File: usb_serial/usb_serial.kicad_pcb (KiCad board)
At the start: 2 copper layers, 17 parts, among them P1 USB_OTG, P2 CONN_01X04, P3 CONN_01X04, Q1 S8050, Q2 S8050, U1 CH340G, X1 CRYSTAL_SMD

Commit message: Unsaved changes
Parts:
- C2: value C -> 100nF
- D1: value D_Schottky -> D_Schottky_x2_ACom_AKK; footprint Diodes_SMD:DO-214AB_Handsoldering -> TO_SOT_Packages_SMD:SOT-23
- moved P2 37.1 mm to (147.2, 78.5)
- moved P3 32.0 mm to (167.6, 78.5)
- moved D1 1.84 mm to (190.6, 121.7)
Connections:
- D1 pad 1: +5V -> +5P
- D1 pad 2: +5P -> Net-(D1-Pad2)
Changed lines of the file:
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@@
     (zones 0)
     (modules 17)
-    (nets 25)
+    (nets 26)
   )
   (page A4)
@@
   (net 23 "Net-(U1-Pad10)")
   (net 24 "Net-(U1-Pad9)")
+  (net 25 "Net-(D1-Pad2)")
   (net_class Default "This is the default net class."
     (clearance 0.2)
@@
     (add_net "Net-(C2-Pad1)")
     (add_net "Net-(C3-Pad1)")
+    (add_net "Net-(D1-Pad2)")
     (add_net "Net-(P1-Pad4)")
     (add_net "Net-(Q1-Pad2)")
@@
       (effects (font (size 1 1) (thickness 0.15)))
     )
-    (fp_text value C (at 0 1.7) (layer F.Fab)
+    (fp_text value 100nF (at 0 1.7) (layer F.Fab)
       (effects (font (size 1 1) (thickness 0.15)))
     )
@@
       (at (xyz 0 0 0))
       (scale (xyz 1 1 1))
-      (rotate (xyz 0 0 180))
-    )
-  )
-  (module Diodes_SMD:DO-214AB_Handsoldering (layer F.Cu)
-    (at 191.387001 120.079)
-    (descr "Jedec DO-214AB diode package. Designed according to Fairchild SS32 datasheet.")
-    (tags "DO-214AB diode Handsoldering")
-    (attr smd)
-    (fp_text reference D1 (at 0 -4.2) (layer F.SilkS)
-      (effects (font (size 1 1) (thickness 0.15)))
-    )
-    (fp_text value D_Schottky (at 0 4.6) (layer F.Fab)
-      (effects (font (size 1 1) (thickness 0.15)))
-    )
-    (fp_line (start -6.15 -3.45) (end 6.15 -3.45) (layer F.CrtYd) (width 0.05))
-    (fp_line (start 6.15 -3.45) (end 6.15 3.45) (layer F.CrtYd) (width 0.05))
-    (fp_line (start 6.15 3.45) (end -6.15 3.45) (layer F.CrtYd) (width 0.05))
-    (fp_line (start -6.15 3.45) (end -6.15 -3.45) (layer F.CrtYd) (width 0.05))
-    (fp_line (start 3.5 3.2) (end -5.8 3.2) (layer F.SilkS) (width 0.15))
-    (fp_line (start -5.8 -3.2) (end 3.5 -3.2) (layer F.SilkS) (width 0.15))
-    (pad 2 smd rect (at 4.1 0) (size 3.6 3.2) (layers F.Cu F.Paste F.Mask)
-      (net 6 +5P))
-    (pad 1 smd rect (at -4.1 0) (size 3.6 3.2) (layers F.Cu F.Paste F.Mask)
-      (net 5 +5V))
-    (model Diodes_SMD.3dshapes/DO-214AB_Handsoldering.wrl
-      (at (xyz 0 0 0))
-      (scale (xyz 0.39 0.39 0.39))
       (rotate (xyz 0 0 180))
     )
@@
   )
   (module Pin_Headers:Pin_Header_Straight_1x04 (layer F.Cu)
-    (at 169.700333 108.079)
+    (at 147.25 78.5)
     (descr "Through hole pin header")
     (tags "pin header")
@@
   )
   (module Pin_Headers:Pin_Header_Straight_1x04 (layer F.Cu)
-    (at 179.910333 108.079)
+    (at 167.57 78.5)
     (descr "Through hole pin header")
     (tags "pin header")
@@
       (at (xyz 0 0 0))
       (scale (xyz 1 1 1))
+      (rotate (xyz 0 0 0))
+    )
+  )
+  (module TO_SOT_Packages_SMD:SOT-23 (layer F.Cu)
+    (at 190.58 121.73)
+    (descr "SOT-23, Standard")
+    (tags SOT-23)
+    (attr smd)
+    (fp_text reference D1 (at 0 -2.25) (layer F.SilkS)
+      (effects (font (size 1 1) (thickness 0.15)))
+    )
+    (fp_text value D_Schottky_x2_ACom_AKK (at 0 2.3) (layer F.Fab)
+      (effects (font (size 1 1) (thickness 0.15)))
+    )
+    (fp_line (start -1.65 -1.6) (end 1.65 -1.6) (layer F.CrtYd) (width 0.05))
+    (fp_line (start 1.65 -1.6) (end 1.65 1.6) (layer F.CrtYd) (width 0.05))
+    (fp_line (start 1.65 1.6) (end -1.65 1.6) (layer F.CrtYd) (width 0.05))
+    (fp_line (start -1.65 1.6) (end -1.65 -1.6) (layer F.CrtYd) (width 0.05))
+    (fp_line (start 1.29916 -0.65024) (end 1.2509 -0.65024) (layer F.SilkS) (width 0.15))
+    (fp_line (start -1.49982 0.0508) (end -1.49982 -0.65024) (layer F.SilkS) (width 0.15))
+    (fp_line (start -1.49982 -0.65024) (end -1.2509 -0.65024) (layer F.SilkS) (width 0.15))
+    (fp_line (start 1.29916 -0.65024) (end 1.49982 -0.65024) (layer F.SilkS) (width 0.15))
+    (fp_line (start 1.49982 -0.65024) (end 1.49982 0.0508) (layer F.SilkS) (width 0.15))
+    (pad 1 smd rect (at -0.95 1.00076) (size 0.8001 0.8001) (layers F.Cu F.Paste F.Mask)
+      (net 6 +5P))
+    (pad 2 smd rect (at 0.95 1.00076) (size 0.8001 0.8001) (layers F.Cu F.Paste F.Mask)
+      (net 25 "Net-(D1-Pad2)"))
+    (pad 3 smd rect (at 0 -0.99822) (size 0.8001 0.8001) (layers F.Cu F.Paste F.Mask)
+      (net 5 +5V))
+    (model TO_SOT_Packages_SMD.3dshapes/SOT-23.wrl
+      (at (xyz 0 0 0))
+      (scale (xyz 1 1 1))

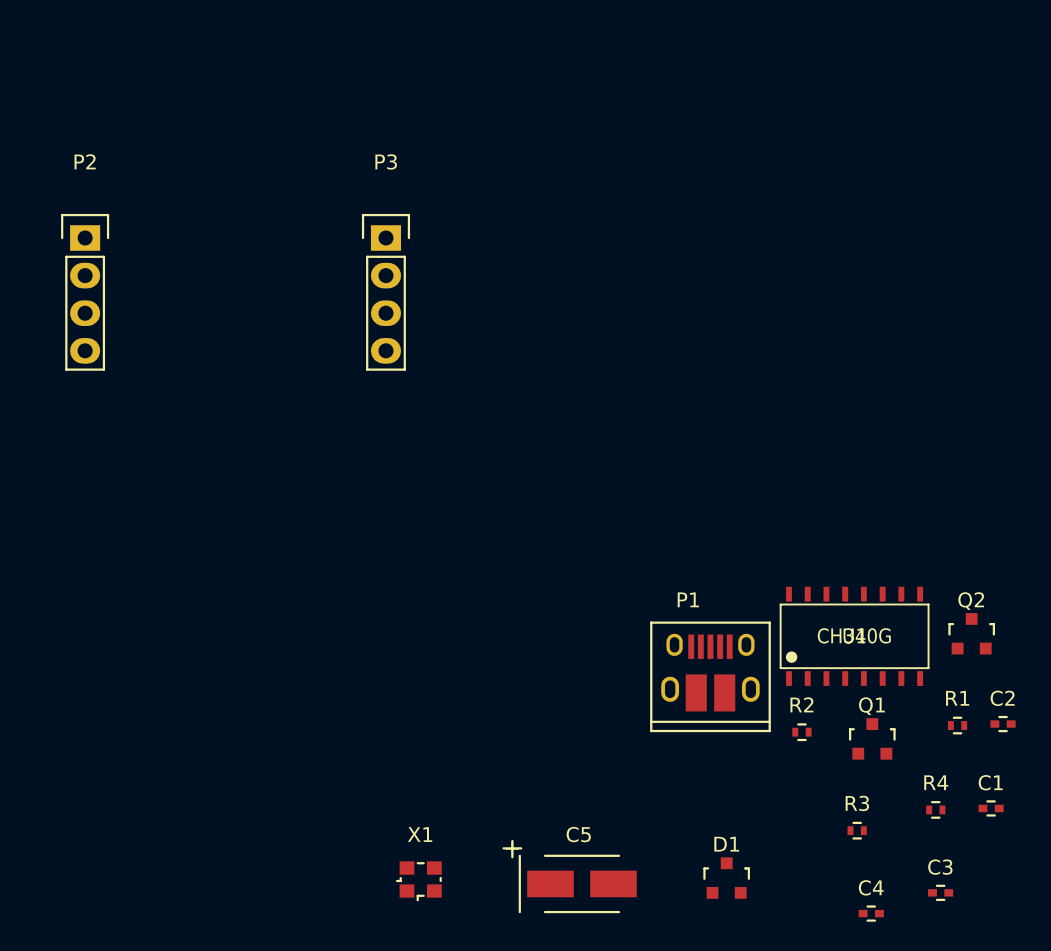
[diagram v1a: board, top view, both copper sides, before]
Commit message: Fixed S8050 footprints. USB PCB v0. Pending GND filled zone.
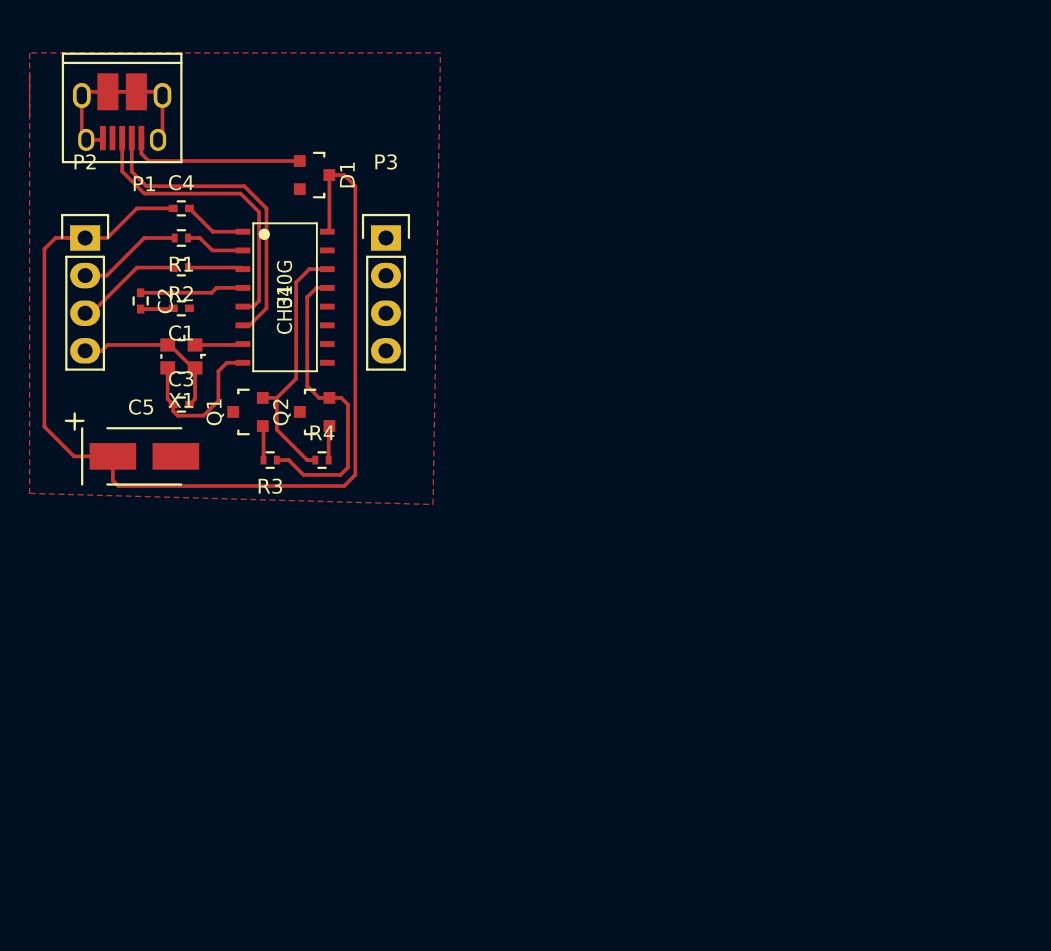
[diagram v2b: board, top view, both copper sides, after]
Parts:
- Q1, Q2: footprint TO_SOT_Packages_SMD:SOT-23 -> SOT-23_S8050:SOT-23_S8050
- moved C4 66.6 mm to (153.8, 76.5)
- moved C2 64.9 mm to (151.0, 82.8), turned to 270 degrees
- moved C1 64.3 mm to (153.8, 83.2), turned to 180 degrees
- moved R1 61.9 mm to (153.8, 78.5), turned to 180 degrees
- moved C3 61.0 mm to (153.8, 89.8)
- moved D1 55.0 mm to (162.8, 74.2), turned to 270 degrees
- moved P1 54.5 mm to (149.8, 70.2), turned to 180 degrees
- moved R2 52.4 mm to (153.8, 80.5), turned to 180 degrees
- moved R4 47.7 mm to (163.2, 93.5)
- moved Q1 47.6 mm to (158.2, 90.2), turned to 90 degrees
- moved R3 46.9 mm to (159.8, 93.5), turned to 180 degrees
- moved Q2 46.8 mm to (162.8, 90.2), turned to 90 degrees
- moved U1 44.8 mm to (160.8, 82.5), turned to 270 degrees
- moved C5 41.3 mm to (151.2, 93.2)
- moved X1 38.9 mm to (153.8, 86.5), turned to 180 degrees
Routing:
- net +5V: track 0.00 -> 71.2 mm
- net Earth: track 0.00 -> 30.8 mm
- net D_NEG: track 0.00 -> 21.2 mm
- net DTR: track 0.00 -> 20.6 mm
- net D_POS: track 0.00 -> 19.9 mm
- net RTS: track 0.00 -> 17.4 mm
- net +5P: track 0.00 -> 12.0 mm
- net Net-(C3-Pad1): track 0.00 -> 10.6 mm
- net RX: track 0.00 -> 7.33 mm
- net TX: track 0.00 -> 7.10 mm
- net Net-(C2-Pad1): track 0.00 -> 7.04 mm
- net Net-(R1-Pad1): track 0.00 -> 4.05 mm
- net Net-(R2-Pad1): track 0.00 -> 3.75 mm
- net Net-(C1-Pad1): track 0.00 -> 3.25 mm
- net Net-(Q2-Pad2): track 0.00 -> 2.39 mm
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- added copper zone on F.Cu, net Earth

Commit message: Breakout USB v0 done.
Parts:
- moved C4 0.50 mm to (153.8, 77.0)
- moved R1 0.50 mm to (153.8, 79.0)
- moved R2 0.50 mm to (153.8, 81.0)
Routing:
- net Earth: track 30.8 -> 41.3 mm
- net +5V: track 71.2 -> 69.7 mm
- net D_NEG: track 21.2 -> 20.7 mm
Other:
- board outline added: 25.2 x 30.5 mm

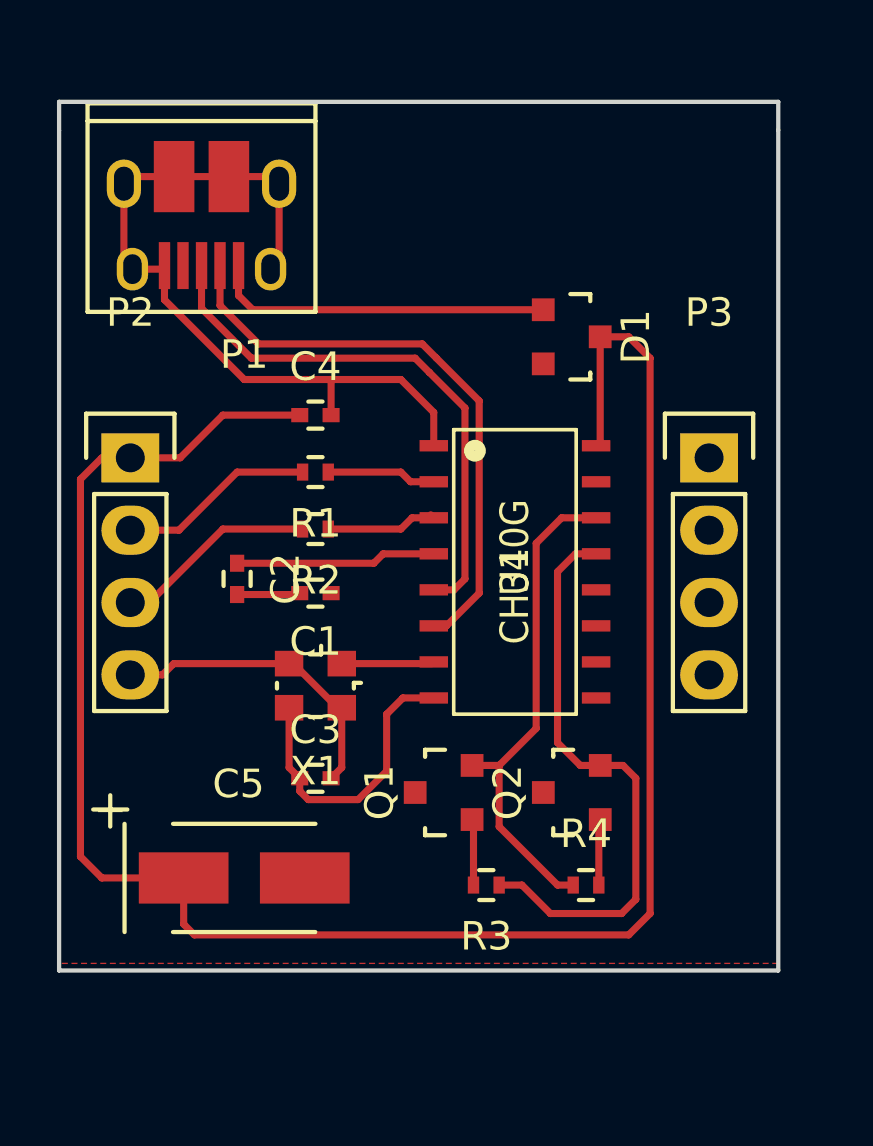
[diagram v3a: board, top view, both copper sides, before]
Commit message: Mounting holes & silkscreen with labels
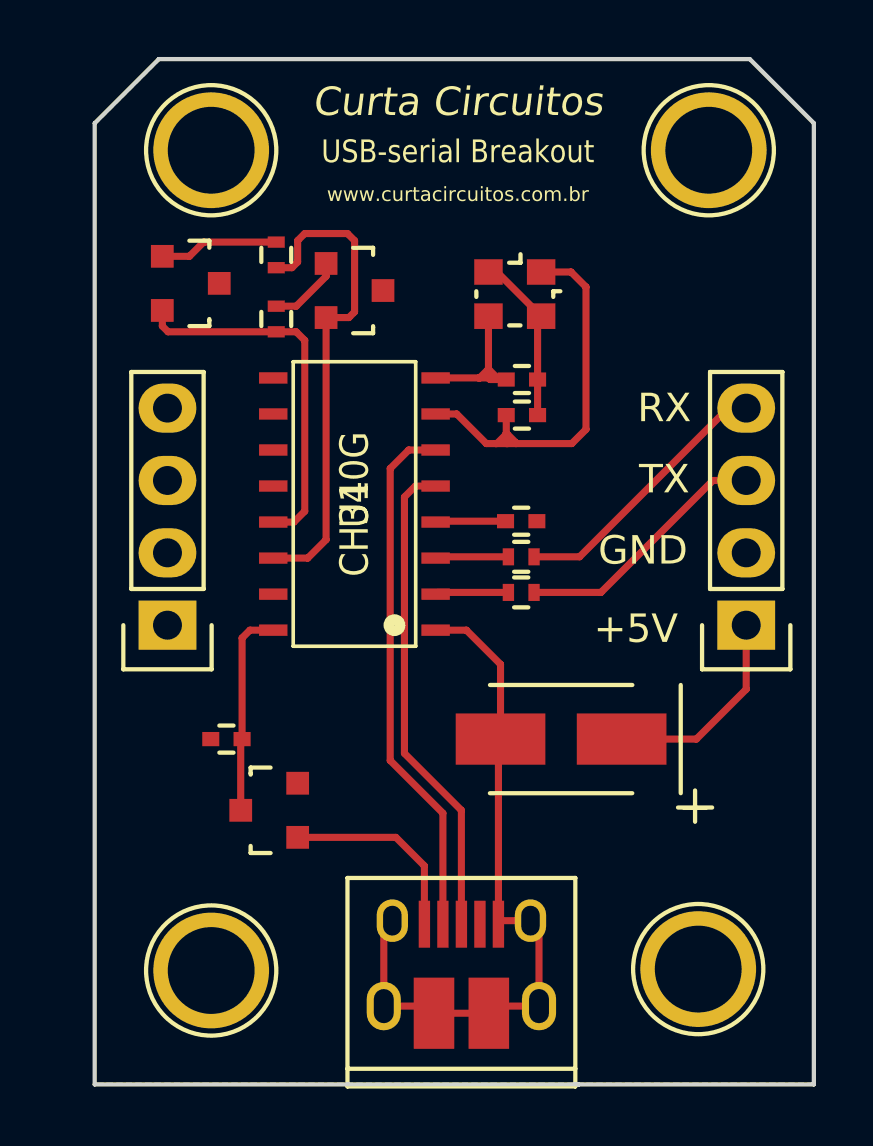
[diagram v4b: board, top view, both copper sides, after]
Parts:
- added REF**: 1pin, Connect:1pin, F.Cu at (150.1, 67.7)
- added REF**: 1pin, Connect:1pin, F.Cu at (167.6, 67.7)
- added REF**: 1pin, Connect:1pin, F.Cu at (167.2, 96.5)
- added REF**: 1pin, Connect:1pin, F.Cu at (150.1, 96.5)
- moved P1 27.7 mm to (158.9, 96.4), turned to 0 degrees
- moved R4 24.7 mm to (152.4, 71.4), turned to 90 degrees
- moved P2 22.4 mm to (168.9, 84.4), turned to 180 degrees
- moved Q2 22.3 mm to (149.4, 72.4), turned to 270 degrees
- moved R3 21.2 mm to (152.4, 73.6), turned to 90 degrees
- moved P3 19.9 mm to (148.6, 84.4), turned to 180 degrees
- moved D1 19.7 mm to (152.1, 90.9), turned to 90 degrees
- moved Q1 17.9 mm to (155.1, 72.6), turned to 270 degrees
- moved C3 15.8 mm to (161.0, 75.8)
- moved X1 15.4 mm to (160.8, 72.8)
- moved C5 12.1 mm to (162.4, 88.4), turned to 180 degrees
- moved C4 11.8 mm to (150.6, 88.4), turned to 180 degrees
- moved C2 10.2 mm to (161.0, 80.7), turned to 0 degrees
- moved C1 9.57 mm to (161.0, 77.0), turned to 0 degrees
- moved R1 8.37 mm to (161.0, 83.2), turned to 0 degrees
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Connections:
- P2 pad 2: TX -> Earth
- P2 pad 3: RX -> TX
- P2 pad 4: Earth -> RX
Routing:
- net +5V: track 69.7 -> 14.6 mm
- net Net-(C1-Pad1): track 3.25 -> 14.8 mm
- net Earth: track 41.3 -> 31.1 mm
- net DTR: track 20.6 -> 13.0 mm
- net +5P: track 12.0 -> 6.91 mm
- net Net-(C2-Pad1): track 7.04 -> 2.47 mm
- net Net-(C3-Pad1): track 10.6 -> 6.29 mm
- net D_POS: track 19.5 -> 17.1 mm
- net TX: track 6.89 -> 9.08 mm
- net D_NEG: track 20.7 -> 18.6 mm
- net RX: track 7.54 -> 9.61 mm
- net Net-(Q2-Pad2): track 2.39 -> 4.21 mm
- net Net-(R2-Pad1): track 4.02 -> 2.57 mm
- net Net-(R1-Pad1): track 3.85 -> 2.58 mm
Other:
- board size 25.2 x 30.5 mm -> 25.2 x 36 mm
- board text added: "+5V"
- board text added: "Curta Circuitos"
- board text added: "GND"
- board text added: "RX"
- board text added: "TX"
- board text added: "USB-serial Breakout"
- board text added: "www.curtacircuitos.com.br"

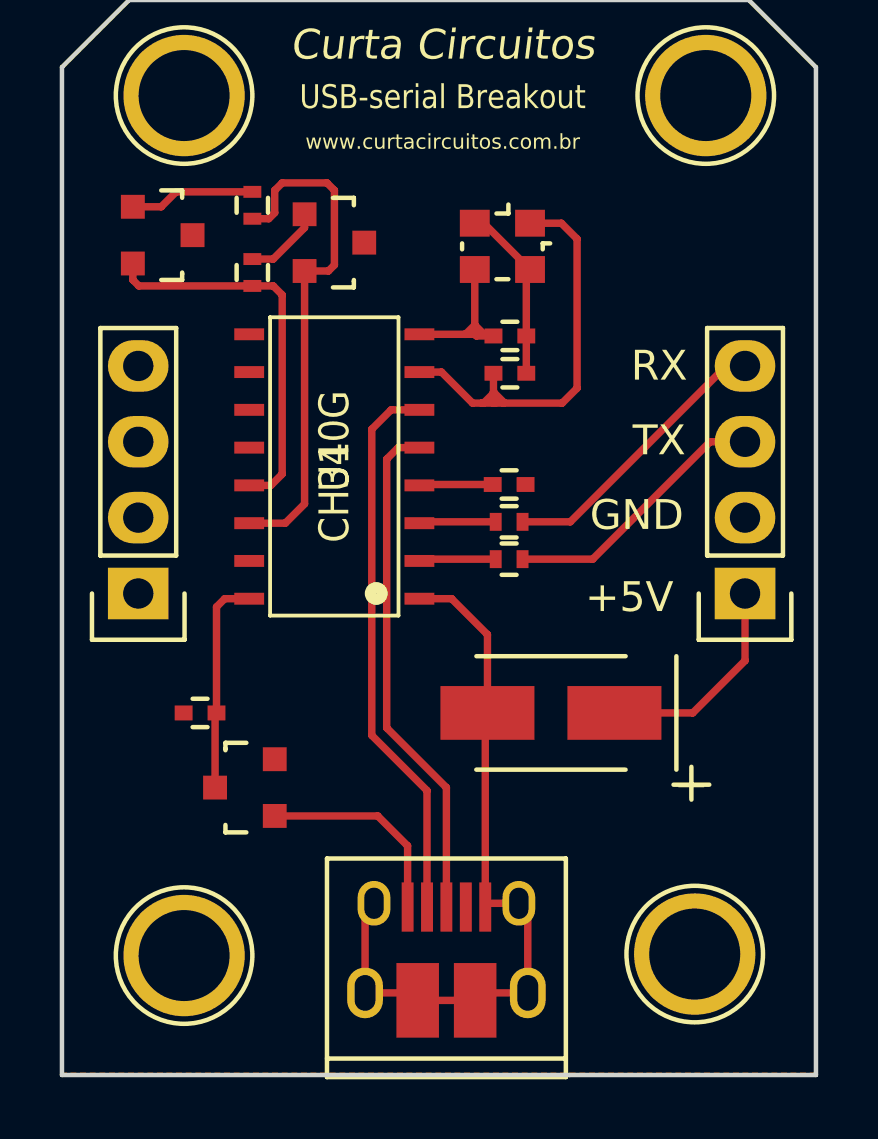
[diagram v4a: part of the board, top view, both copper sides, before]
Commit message: Expanded pin headers and minor fixes. Pics updated.
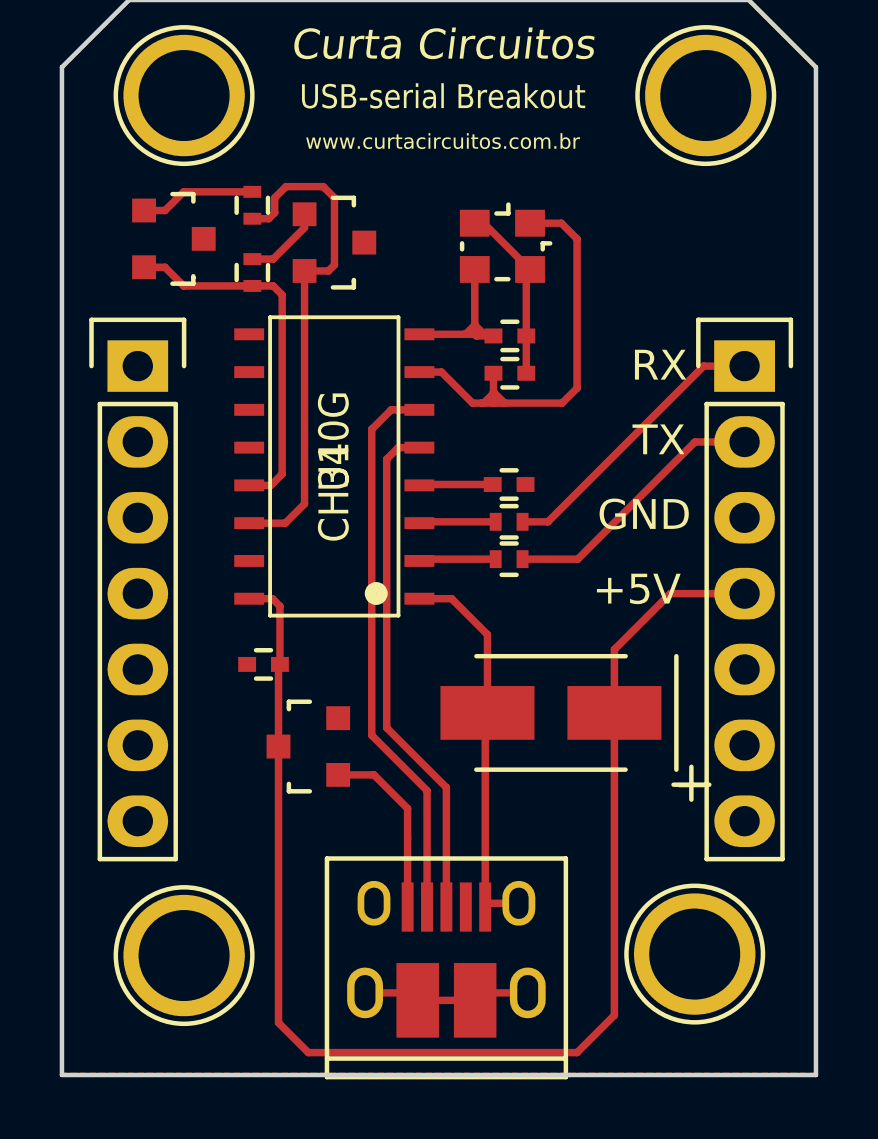
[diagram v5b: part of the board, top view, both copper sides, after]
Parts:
- P2, P3: value CONN_01X04 -> CONN_01X07; footprint Pin_Headers:Pin_Header_Straight_1x04 -> Pin_Headers:Pin_Header_Straight_1x07
- moved P2 7.62 mm to (168.9, 76.8), turned to 0 degrees
- moved P3 7.62 mm to (148.5, 76.8), turned to 0 degrees
- moved C4 2.68 mm to (152.8, 86.8)
- moved D1 2.53 mm to (154.2, 89.5)
- moved Q2 0.40 mm to (149.8, 72.5)
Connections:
- P2 pad 1: +5V -> RX
- P2 pad 2: Earth -> TX
- P2 pad 3: TX -> Earth
- P2 pad 4: RX -> +5V
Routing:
- net +5V: track 14.6 -> 44.7 mm
- net Earth: track 31.1 -> 25.6 mm
- net +5P: track 6.91 -> 6.09 mm
- net DTR: track 13.0 -> 12.3 mm
- net RX: track 9.61 -> 10.2 mm
